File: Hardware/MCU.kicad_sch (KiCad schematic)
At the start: 1 part, among them U1 STM32F722ZETx

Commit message: Checkpoint
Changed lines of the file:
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@@
     (effects (font (size 1.27 1.27)) (justify left))
   )
-  (hierarchical_label "TIM12_CH1" (shape input) (at 281.94 83.82 0) (fields_autoplaced)
+  (hierarchical_label "TIM9_CH2" (shape input) (at 281.94 83.82 0) (fields_autoplaced)
     (effects (font (size 1.27 1.27)) (justify left))
   )
@@
     (effects (font (size 1.27 1.27)) (justify left))
   )
+  (hierarchical_label "GPIO_PE15" (shape output) (at 304.8 106.68 0) (fields_autoplaced)
+    (effects (font (size 1.27 1.27)) (justify left))
+  )
   (hierarchical_label "TIM1_CH4" (shape output) (at 228.6 104.14 0) (fields_autoplaced)
     (effects (font (size 1.27 1.27)) (justify left))
@@
     (effects (font (size 1.27 1.27)) (justify left))
   )
-  (hierarchical_label "I2C1_SCL" (shape bidirectional) (at 355.6 53.34 0) (fields_autoplaced)
+  (hierarchical_label "I2C2_SCL" (shape bidirectional) (at 355.6 53.34 0) (fields_autoplaced)
     (effects (font (size 1.27 1.27)) (justify left))
   )
@@
     (effects (font (size 1.27 1.27)) (justify left))
   )
+  (hierarchical_label "SPI2_MOSI" (shape output) (at 304.8 101.6 0) (fields_autoplaced)
+    (effects (font (size 1.27 1.27)) (justify left))
+  )
   (hierarchical_label "RTC_OUT" (shape output) (at 228.6 58.42 0) (fields_autoplaced)
     (effects (font (size 1.27 1.27)) (justify left))
@@
     (effects (font (size 1.27 1.27)) (justify left))
   )
+  (hierarchical_label "UART5_RX" (shape input) (at 355.6 68.58 0) (fields_autoplaced)
+    (effects (font (size 1.27 1.27)) (justify left))
+  )
   (hierarchical_label "TIM3_CH4" (shape output) (at 228.6 93.98 0) (fields_autoplaced)
     (effects (font (size 1.27 1.27)) (justify left))
@@
     (effects (font (size 1.27 1.27)) (justify left))
   )
-  (hierarchical_label "USART1_RX" (shape input) (at 355.6 144.78 0) (fields_autoplaced)
-    (effects (font (size 1.27 1.27)) (justify left))
-  )
-  (hierarchical_label "GPIO_PB15+RTC_REFIN" (shape input) (at 355.6 81.28 0) (fields_autoplaced)
+  (hierarchical_label "GPIO_PD5+EXTI5" (shape input) (at 355.6 81.28 0) (fields_autoplaced)
     (effects (font (size 1.27 1.27)) (justify left))
   )
@@
     (effects (font (size 1.27 1.27)) (justify left))
   )
-  (hierarchical_label "UART8_TX" (shape output) (at 355.6 71.12 0) (fields_autoplaced)
-    (effects (font (size 1.27 1.27)) (justify left))
-  )
-  (hierarchical_label "USART1_TX" (shape output) (at 355.6 142.24 0) (fields_autoplaced)
-    (effects (font (size 1.27 1.27)) (justify left))
-  )
-  (hierarchical_label "GPIO_PG15" (shape output) (at 355.6 76.2 0) (fields_autoplaced)
+  (hierarchical_label "UART8_TX" (shape output) (at 355.6 144.78 0) (fields_autoplaced)
+    (effects (font (size 1.27 1.27)) (justify left))
+  )
+  (hierarchical_label "GPIO_PD0" (shape output) (at 355.6 76.2 0) (fields_autoplaced)
     (effects (font (size 1.27 1.27)) (justify left))
   )
@@
     (effects (font (size 1.27 1.27)) (justify left))
   )
-  (hierarchical_label "GPIO_PC1+EXTI1+SYS_WKUP3" (shape bidirectional) (at 281.94 63.5 0) (fields_autoplaced)
-    (effects (font (size 1.27 1.27)) (justify left))
-  )
-  (hierarchical_label "TIM13_CH1" (shape output) (at 281.94 88.9 0) (fields_autoplaced)
+  (hierarchical_label "GPIO_PC1+EXTI1" (shape bidirectional) (at 281.94 63.5 0) (fields_autoplaced)
+    (effects (font (size 1.27 1.27)) (justify left))
+  )
+  (hierarchical_label "TIM11_CH1" (shape output) (at 281.94 88.9 0) (fields_autoplaced)
     (effects (font (size 1.27 1.27)) (justify left))
   )
@@
     (effects (font (size 1.27 1.27)) (justify left))
   )
-  (hierarchical_label "ADC1_IN4" (shape input) (at 228.6 66.04 0) (fields_autoplaced)
+  (hierarchical_label "ADC1_IN10" (shape input) (at 228.6 66.04 0) (fields_autoplaced)
     (effects (font (size 1.27 1.27)) (justify left))
   )
@@
     (effects (font (size 1.27 1.27)) (justify left))
   )
+  (hierarchical_label "USB_OTG_HS_VBUS" (shape bidirectional) (at 304.8 182.88 0) (fields_autoplaced)
+    (effects (font (size 1.27 1.27)) (justify left))
+  )
   (hierarchical_label "VBAT" (shape passive) (at 228.6 53.34 0) (fields_autoplaced)
     (effects (font (size 1.27 1.27)) (justify left))
   )
-  (hierarchical_label "I2C1_SDA" (shape bidirectional) (at 355.6 50.8 0) (fields_autoplaced)
-    (effects (font (size 1.27 1.27)) (justify left))
-  )
-  (hierarchical_label "GPIO_PA0+EXTI0+SYS_WKUP1+TIM2_CH1+TIM2_ETR+TIM5_CH1" (shape bidirectional)
-    (at 281.94 66.04 0) (fields_autoplaced)
+  (hierarchical_label "USB_OTG_HS_DM" (shape bidirectional) (at 304.8 180.34 0) (fields_autoplaced)
+    (effects (font (size 1.27 1.27)) (justify left))
+  )
+  (hierarchical_label "I2C2_SDA" (shape bidirectional) (at 355.6 50.8 0) (fields_autoplaced)
+    (effects (font (size 1.27 1.27)) (justify left))
+  )
+  (hierarchical_label "GPIO_PA0+EXTI0+TIM2_CH1+TIM2_ETR+TIM5_CH1" (shape bidirectional) (at 281.94 66.04 0) (fields_autoplaced)
     (effects (font (size 1.27 1.27)) (justify left))
   )
@@
     (effects (font (size 1.27 1.27)) (justify left))
   )
-  (hierarchical_label "GPIO_PA2+EXTI2+SYS_WKUP2+TIM2_CH2+TIM5_CH3+USART2_TX" (shape bidirectional)
-    (at 281.94 68.58 0) (fields_autoplaced)
+  (hierarchical_label "GPIO_PA2+EXTI2+TIM2_CH2+TIM5_CH3+USART2_TX" (shape bidirectional) (at 281.94 68.58 0) (fields_autoplaced)
+    (effects (font (size 1.27 1.27)) (justify left))
+  )
+  (hierarchical_label "GPIO_PB11+EXTI11" (shape input) (at 304.8 109.22 0) (fields_autoplaced)
     (effects (font (size 1.27 1.27)) (justify left))
   )
@@
     (effects (font (size 1.27 1.27)) (justify left))
   )
+  (hierarchical_label "SPI2_MISO" (shape input) (at 304.8 99.06 0) (fields_autoplaced)
+    (effects (font (size 1.27 1.27)) (justify left))
+  )
   (hierarchical_label "ADC1_IN15" (shape input) (at 228.6 71.12 0) (fields_autoplaced)
     (effects (font (size 1.27 1.27)) (justify left))
   )
+  (hierarchical_label "UART5_TX" (shape output) (at 355.6 71.12 0) (fields_autoplaced)
+    (effects (font (size 1.27 1.27)) (justify left))
+  )
   (hierarchical_label "SPI4_MISO" (shape input) (at 281.94 55.88 0) (fields_autoplaced)
     (effects (font (size 1.27 1.27)) (justify left))
@@
     (effects (font (size 1.27 1.27)) (justify left))
   )
+  (hierarchical_label "USB_OTG_HS_DP" (shape bidirectional) (at 304.8 177.8 0) (fields_autoplaced)
+    (effects (font (size 1.27 1.27)) (justify left))
+  )
+  (hierarchical_label "SPI2_SCK" (shape output) (at 304.8 104.14 0) (fields_autoplaced)
+    (effects (font (size 1.27 1.27)) (justify left))
+  )
   (hierarchical_label "TIM4_CH2" (shape output) (at 228.6 109.22 0) (fields_autoplaced)
     (effects (font (size 1.27 1.27)) (justify left))
@@
     (effects (font (size 1.27 1.27)) (justify left))
   )
-  (hierarchical_label "UART8_RX" (shape input) (at 355.6 68.58 0) (fields_autoplaced)
-    (effects (font (size 1.27 1.27)) (justify left))
-  )
+  (hierarchical_label "UART8_RX" (shape input) (at 355.6 142.24 0) (fields_autoplaced)
+    (effects (font (size 1.27 1.27)) (justify left))
+  )

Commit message: Checkpoint
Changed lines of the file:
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@@
     (effects (font (size 1.27 1.27)) (justify left))
   )
-  (hierarchical_label "GPIO_PG1" (shape output) (at 228.6 60.96 0) (fields_autoplaced)
+  (hierarchical_label "GPIO_PG1" (shape output) (at 228.6 58.42 0) (fields_autoplaced)
     (effects (font (size 1.27 1.27)) (justify left))
   )
@@
     (effects (font (size 1.27 1.27)) (justify left))
   )
-  (hierarchical_label "VDD" (shape passive) (at 228.6 50.8 0) (fields_autoplaced)
+  (hierarchical_label "VDD" (shape passive) (at 228.6 48.26 0) (fields_autoplaced)
     (effects (font (size 1.27 1.27)) (justify left))
   )
   (hierarchical_label "ADC3_IN9" (shape input) (at 228.6 76.2 0) (fields_autoplaced)
+    (effects (font (size 1.27 1.27)) (justify left))
+  )
+  (hierarchical_label "GPIO_PG0" (shape output) (at 228.6 60.96 0) (fields_autoplaced)
     (effects (font (size 1.27 1.27)) (justify left))
   )
@@
     (effects (font (size 1.27 1.27)) (justify left))
   )
-  (hierarchical_label "RTC_OUT" (shape output) (at 228.6 58.42 0) (fields_autoplaced)
+  (hierarchical_label "RTC_OUT" (shape output) (at 228.6 55.88 0) (fields_autoplaced)
     (effects (font (size 1.27 1.27)) (justify left))
   )
@@
     (effects (font (size 1.27 1.27)) (justify left))
   )
-  (hierarchical_label "VBAT" (shape passive) (at 228.6 53.34 0) (fields_autoplaced)
+  (hierarchical_label "VBAT" (shape passive) (at 228.6 50.8 0) (fields_autoplaced)
     (effects (font (size 1.27 1.27)) (justify left))
   )

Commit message: Checkpoint
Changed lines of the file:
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@@
     (effects (font (size 1.27 1.27)) (justify left))
   )
-  (hierarchical_label "GPIO_PG1" (shape output) (at 228.6 58.42 0) (fields_autoplaced)
+  (hierarchical_label "GPIO_PG2" (shape output) (at 228.6 48.26 0) (fields_autoplaced)
     (effects (font (size 1.27 1.27)) (justify left))
   )
@@
     (effects (font (size 1.27 1.27)) (justify left))
   )
-  (hierarchical_label "VDD" (shape passive) (at 228.6 48.26 0) (fields_autoplaced)
+  (hierarchical_label "VDD" (shape passive) (at 228.6 38.1 0) (fields_autoplaced)
     (effects (font (size 1.27 1.27)) (justify left))
   )
@@
     (effects (font (size 1.27 1.27)) (justify left))
   )
-  (hierarchical_label "GPIO_PG0" (shape output) (at 228.6 60.96 0) (fields_autoplaced)
+  (hierarchical_label "GPIO_PG3" (shape output) (at 228.6 50.8 0) (fields_autoplaced)
     (effects (font (size 1.27 1.27)) (justify left))
   )
@@
   )
   (hierarchical_label "QUADSPI_CLK" (shape output) (at 304.8 152.4 0) (fields_autoplaced)
+    (effects (font (size 1.27 1.27)) (justify left))
+  )
+  (hierarchical_label "GPIO_PG5" (shape input) (at 228.6 55.88 0) (fields_autoplaced)
     (effects (font (size 1.27 1.27)) (justify left))
   )
@@
     (effects (font (size 1.27 1.27)) (justify left))
   )
-  (hierarchical_label "RTC_OUT" (shape output) (at 228.6 55.88 0) (fields_autoplaced)
+  (hierarchical_label "RTC_OUT" (shape output) (at 228.6 45.72 0) (fields_autoplaced)
     (effects (font (size 1.27 1.27)) (justify left))
   )
@@
     (effects (font (size 1.27 1.27)) (justify left))
   )
-  (hierarchical_label "VBAT" (shape passive) (at 228.6 50.8 0) (fields_autoplaced)
+  (hierarchical_label "VBAT" (shape passive) (at 228.6 40.64 0) (fields_autoplaced)
     (effects (font (size 1.27 1.27)) (justify left))
   )
@@
     (effects (font (size 1.27 1.27)) (justify left))
   )
+  (hierarchical_label "GPIO_PG4" (shape output) (at 228.6 53.34 0) (fields_autoplaced)
+    (effects (font (size 1.27 1.27)) (justify left))
+  )

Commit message: Checkpoint
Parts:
- added C27, C28, C45: 4.7uF, symbol Device:C_Small
- added C29, C32, C33, C34, C35, C36, C37, C38, C39, C40, C41, C42, C43, C46: 100nF, symbol Device:C_Small
- added C30, C31: pF, symbol Device:C_Small
- added C44, C47: 1uF, symbol Device:C_Small
- added R66: 10K, symbol Device:R_Small
- added SW1: RESET, symbol Switch:SW_Push
- added Y1: 24MHz, symbol Device:Crystal_Small
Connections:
- net ADC1_IN10: now also U1.26 (PC0)
- net ADC1_IN14: now also U1.44 (PC4)
- net ADC1_IN15: now also U1.45 (PC5)
- net ADC3_IN14: now also U1.14 (PF4)
- net ADC3_IN15: now also U1.15 (PF5)
- net ADC3_IN8: now also U1.22 (PF10)
- net ADC3_IN9: now also U1.13 (PF3)
- net GND: now also C27.1, C28.1, C29.1, C30.1, C31.1, C32.2, C33.2, C34.2, C35.2, C36.2, C37.2, C38.2, C39.2, C40.2, C41.2, C42.2, C43.2, C44.2, C45.2, C46.2, C47.2, R66.2, SW1.1
- net GPIO_PA0+EXTI0+TIM2_CH1+TIM2_ETR+TIM5_CH1: now also U1.34 (PA0)
- net GPIO_PA2+EXTI2+TIM2_CH2+TIM5_CH3+USART2_TX: now also U1.36 (PA2)
- net GPIO_PB11+EXTI11: now also U1.70 (PB11)
- net GPIO_PC1+EXTI1: now also U1.27 (PC1)
- net GPIO_PC14+EXTI14: now also U1.8 (PC14)
- net GPIO_PC15+EXTI15: now also U1.9 (PC15)
- net GPIO_PD0: now also U1.114 (PD0)
- net GPIO_PD4+EXTI4: now also U1.118 (PD4)
- net GPIO_PD5+EXTI5: now also U1.119 (PD5)
- net GPIO_PE15: now also U1.68 (PE15)
- net GPIO_PE3+EXTI3: now also U1.2 (PE3)
- net GPIO_PE4: now also U1.3 (PE4)
- net GPIO_PF2: now also U1.12 (PF2)
- net GPIO_PG13: now also U1.128 (PG13)
- net GPIO_PG14: now also U1.129 (PG14)
- net GPIO_PG2: now also U1.87 (PG2)
- net GPIO_PG3: now also U1.88 (PG3)
- net GPIO_PG4: now also U1.89 (PG4)
- net GPIO_PG5: now also U1.90 (PG5)
- net I2C2_SCL: now also U1.11 (PF1)
- net I2C2_SDA: now also U1.10 (PF0)
- net NRST: now also U1.25 (NRST), C29.2, SW1.2
- net QUADSPI_BK1_NCS: now also U1.136 (PB6)
- net QUADSPI_BK2_NCS: now also U1.112 (PC11)
- net QUADSPI_CLK: now also U1.48 (PB2)
- net RTC_OUT: now also U1.7 (PC13)
- net SDMMC2_CK: now also U1.122 (PD6)
- net SDMMC2_CMD: now also U1.123 (PD7)
- net SPI2_MISO: now also U1.28 (PC2)
- net SPI2_MOSI: now also U1.29 (PC3)
- net SPI2_SCK: now also U1.69 (PB10)
- net SPI4_MISO: now also U1.4 (PE5)
- net SPI4_MOSI: now also U1.5 (PE6)
- net SPI4_SCK: now also U1.1 (PE2)
- net SYS_JTCK-SWCLK: now also U1.109 (PA14)
- net SYS_JTDI: now also U1.110 (PA15)
- net SYS_JTDO-SWO: now also U1.133 (PB3)
- net SYS_JTMS-SWDIO: now also U1.105 (PA13)
- net TIM11_CH1: now also U1.140 (PB9)
- net TIM1_CH1: now also U1.100 (PA8)
- net TIM1_CH2: now also U1.101 (PA9)
- net TIM1_CH3: now also U1.102 (PA10)
- net TIM1_CH4: now also U1.103 (PA11)
- net TIM3_CH1+USART6_TX: now also U1.96 (PC6)
- net TIM3_CH2: now also U1.97 (PC7)
- net TIM3_CH3: now also U1.98 (PC8)
- net TIM3_CH4: now also U1.99 (PC9)
- net TIM4_CH1: now also U1.81 (PD12)
- net TIM4_CH2: now also U1.82 (PD13)
- net TIM4_CH3: now also U1.85 (PD14)
- net TIM4_CH4: now also U1.86 (PD15)
- net TIM9_CH2: now also U1.37 (PA3)
- net UART4_TX: now also U1.111 (PC10)
- net UART5_RX: now also U1.116 (PD2)
- net UART5_TX: now also U1.113 (PC12)
- net UART8_RX: now also U1.141 (PE0)
- net UART8_TX: now also U1.142 (PE1)
- net USART3_RX+EXTI9: now also U1.78 (PD9)
- net USART3_TX: now also U1.77 (PD8)
- net USB_OTG_HS_DM: now also U1.75 (PB14)
- net USB_OTG_HS_DP: now also U1.76 (PB15)
- net USB_OTG_HS_VBUS: now also U1.74 (PB13)
- net VBAT: now also U1.6 (VBAT)
- net VDD: now also U1.108 (VDD), U1.121 (VDDSDMMC), U1.131 (VDD), U1.143 (PDR_ON), U1.144 (VDD), U1.17 (VDD), U1.30 (VDD), U1.32 (VREF+), U1.33 (VDDA), U1.39 (VDD), U1.52 (VDD), U1.62 (VDD), U1.72 (VDD), U1.84 (VDD), U1.95 (VDDUSB), C32.1, C33.1, C34.1, C35.1, C36.1, C37.1, C38.1, C39.1, C40.1, C41.1, C42.1, C43.1, C44.1, C45.1, C46.1, C47.1
- net at U1.106 (VCAP_2): now also C27.2
- net SDMMC2_D0: now reaches U1.124 (PG9)
- net SDMMC2_D1: now reaches U1.125 (PG10)
- net SDMMC2_D2: now reaches U1.126 (PG11)
- net SDMMC2_D3: now reaches U1.127 (PG12)
- net BOOT0: now reaches U1.138 (BOOT0)
- net BOOT0: now also R66.1
- net QUADSPI_BK1_IO3: now reaches U1.18 (PF6)
- net QUADSPI_BK1_IO2: now reaches U1.19 (PF7)
- net QUADSPI_BK1_IO0: now reaches U1.20 (PF8)
- net QUADSPI_BK1_IO1: now reaches U1.21 (PF9)
- net at U1.23 (PH0): now also C31.2, Y1.2
- net at U1.24 (PH1): now also C30.2, Y1.1
- net USB_OTG_HS_SOF: now reaches U1.40 (PA4)
- net QUADSPI_BK2_IO0: now reaches U1.58 (PE7)
- net QUADSPI_BK2_IO1: now reaches U1.59 (PE8)
- net QUADSPI_BK2_IO2: now reaches U1.60 (PE9)
- net QUADSPI_BK2_IO3: now reaches U1.63 (PE10)
- net at U1.71 (VCAP_1): now also C28.2
- no-connect marks 0 -> 31
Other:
- note added: "VDD"
- note added: "VDDA"
- note added: "VDDSDMMC"
- moved on the sheet: U1

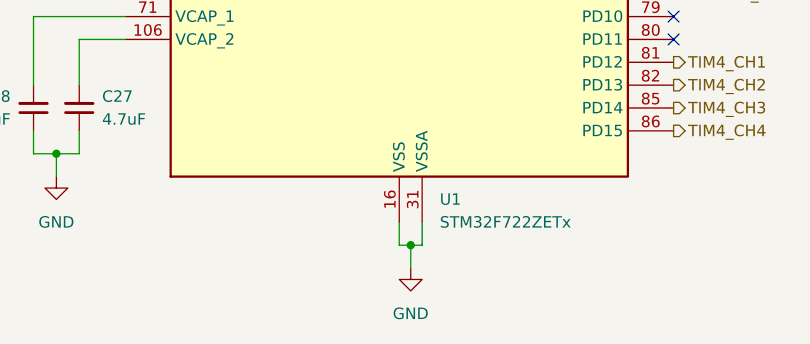
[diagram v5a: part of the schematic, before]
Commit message: ERC fixes
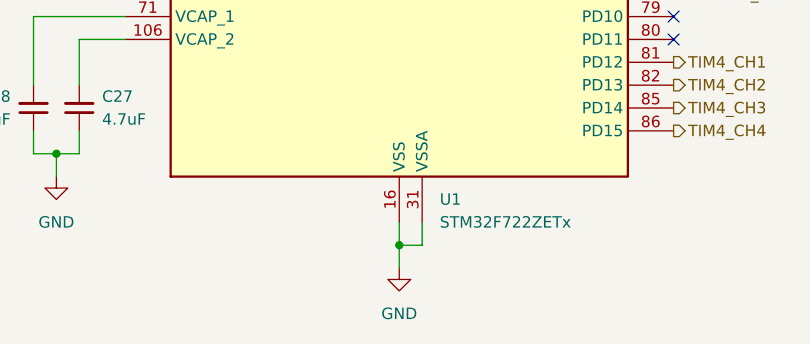
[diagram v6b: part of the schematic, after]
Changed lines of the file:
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@@
   (junction (at 307.34 144.78) (diameter 0) (color 0 0 0 0)
   )
+  (junction (at 152.4 259.08) (diameter 0) (color 0 0 0 0)
+  )
   (junction (at 152.4 68.58) (diameter 0) (color 0 0 0 0)
   )
@@
   )
   (junction (at 320.04 116.84) (diameter 0) (color 0 0 0 0)
-  )
-  (junction (at 153.67 259.08) (diameter 0) (color 0 0 0 0)
   )
   (junction (at 162.56 68.58) (diameter 0) (color 0 0 0 0)
@@
     (stroke (width 0) (type default))
   )
-  (wire (pts (xy 153.67 259.08) (xy 154.94 259.08))
-    (stroke (width 0) (type default))
-  )
   (wire (pts (xy 332.74 88.9) (xy 332.74 86.36))
     (stroke (width 0) (type default))
   )
+  (wire (pts (xy 152.4 259.08) (xy 154.94 259.08))
+    (stroke (width 0) (type default))
+  )
   (wire (pts (xy 76.2 210.82) (xy 121.92 210.82))
     (stroke (width 0) (type default))
@@
     (stroke (width 0) (type default))
   )
-  (wire (pts (xy 153.67 259.08) (xy 152.4 259.08))
-    (stroke (width 0) (type default))
-  )
   (wire (pts (xy 96.52 96.52) (xy 96.52 99.06))
     (stroke (width 0) (type default))
@@
     (stroke (width 0) (type default))
   )
-  (wire (pts (xy 153.67 261.62) (xy 153.67 259.08))
+  (wire (pts (xy 152.4 261.62) (xy 152.4 259.08))
     (stroke (width 0) (type default))
   )
@@
     )
   )
-  (symbol (lib_id "power:GND") (at 153.67 261.62 0) (unit 1)
-    (in_bom yes) (on_board yes) (dnp no) (fields_autoplaced)
-    (property "Reference" "#PWR01" (at 153.67 267.97 0)
-      (effects (font (size 1.27 1.27)) hide)
-    )
-    (property "Value" "GND" (at 153.67 266.7 0)
+  (symbol (lib_id "power:GND") (at 152.4 261.62 0) (unit 1)
+    (in_bom yes) (on_board yes) (dnp no) (fields_autoplaced)
+    (property "Reference" "#PWR01" (at 152.4 267.97 0)
+      (effects (font (size 1.27 1.27)) hide)
+    )
+    (property "Value" "GND" (at 152.4 266.7 0)
       (effects (font (size 1.27 1.27)))
     )
-    (property "Footprint" "" (at 153.67 261.62 0)
-      (effects (font (size 1.27 1.27)) hide)
-    )
-    (property "Datasheet" "" (at 153.67 261.62 0)
-      (effects (font (size 1.27 1.27)) hide)
-    )
+    (property "Footprint" "" (at 152.4 261.62 0)
+      (effects (font (size 1.27 1.27)) hide)
+    )
+    (property "Datasheet" "" (at 152.4 261.62 0)
+      (effects (font (size 1.27 1.27)) hide)
+    )

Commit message: Checkpoint
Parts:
- C301: renamed from C31; value pF -> 15pF; footprint (none) -> Capacitor_SMD:C_0805_2012Metric
- C302: renamed from C30; value pF -> 15pF; footprint (none) -> Capacitor_SMD:C_0805_2012Metric
- Y301: renamed from Y1; footprint (none) -> leptunKicadLib:ATS240C; PN (none) -> ATS240C
- renumbered C28 to C303, C27 to C304, C32 to C305, C36 to C306, C40 to C307, C33 to C308, C37 to C309, C41 to C310, C34 to C311, C38 to C312, C42 to C313, C35 to C314, C39 to C315, C43 to C316, C45 to C317, C46 to C318, C29 to C319, C47 to C320, C44 to C321, R66 to R301, SW1 to SW301, U1 to U301
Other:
- moved on the sheet: C301, C302, Y301
